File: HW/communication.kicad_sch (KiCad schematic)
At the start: 14 parts, among them U1 Si4461, Y1 30M

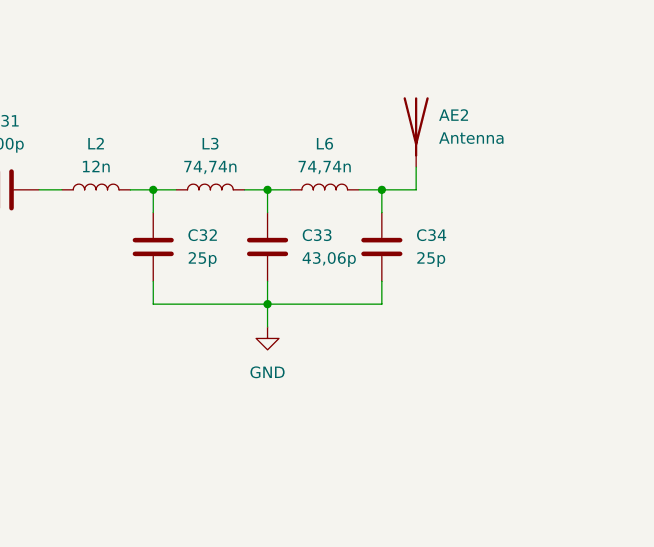
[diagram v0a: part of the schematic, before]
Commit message: impedance matching
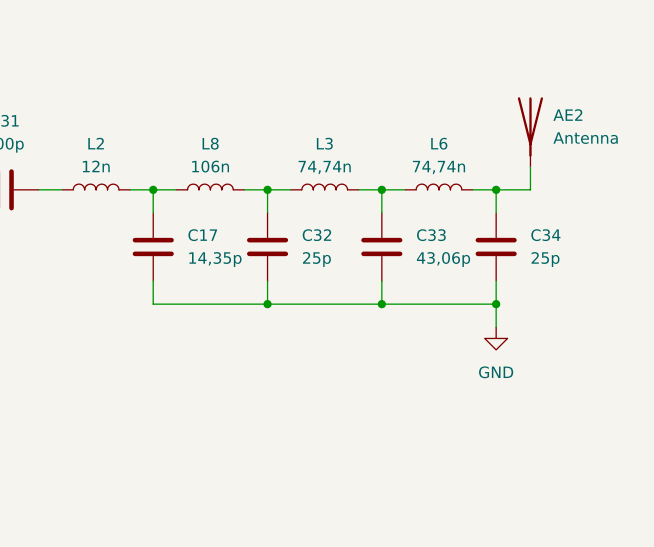
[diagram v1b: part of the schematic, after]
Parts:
- added C17: 14,35p, symbol Device:C
- added L8: 106n, symbol Device:L
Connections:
- net GND: now also C17.1
- net at C32.2, L3.1: now also L8.2; no longer L2.2
- new net: C17.2, L2.2, L8.1
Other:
- moved on the sheet: AE2, C32, C33, C34, L3, L6
